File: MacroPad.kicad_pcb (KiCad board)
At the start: 2 copper layers, 3.6 x 3.3 mm, 42 parts, among them J1 Conn_01x04_Pin, SW1 SW_Push, SW10 SW_Push, SW11 SW_Push, SW12 SW_Push, SW13 RotaryEncoder_Switch, SW14 RotaryEncoder_Switch, SW2 SW_Push, SW3 SW_Push, SW4 SW_Push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

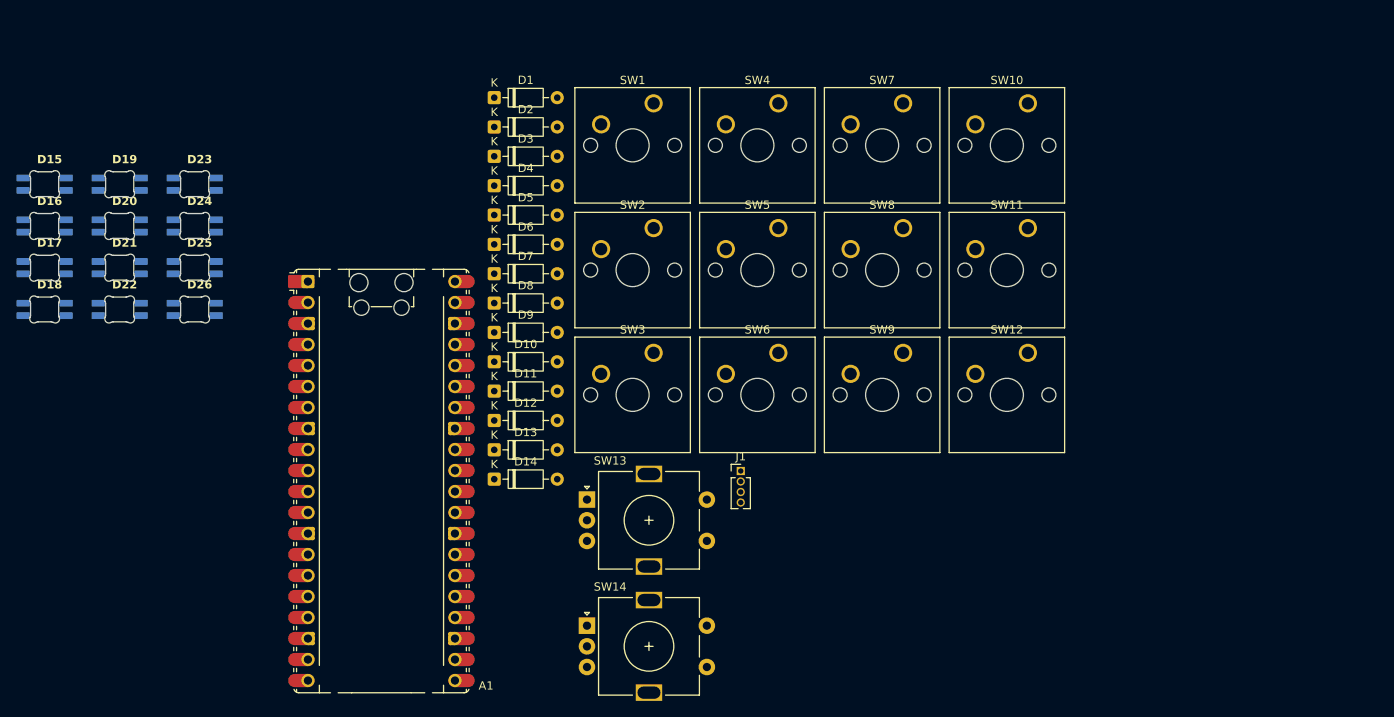
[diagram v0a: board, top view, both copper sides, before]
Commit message: Feat: Designed the PCB
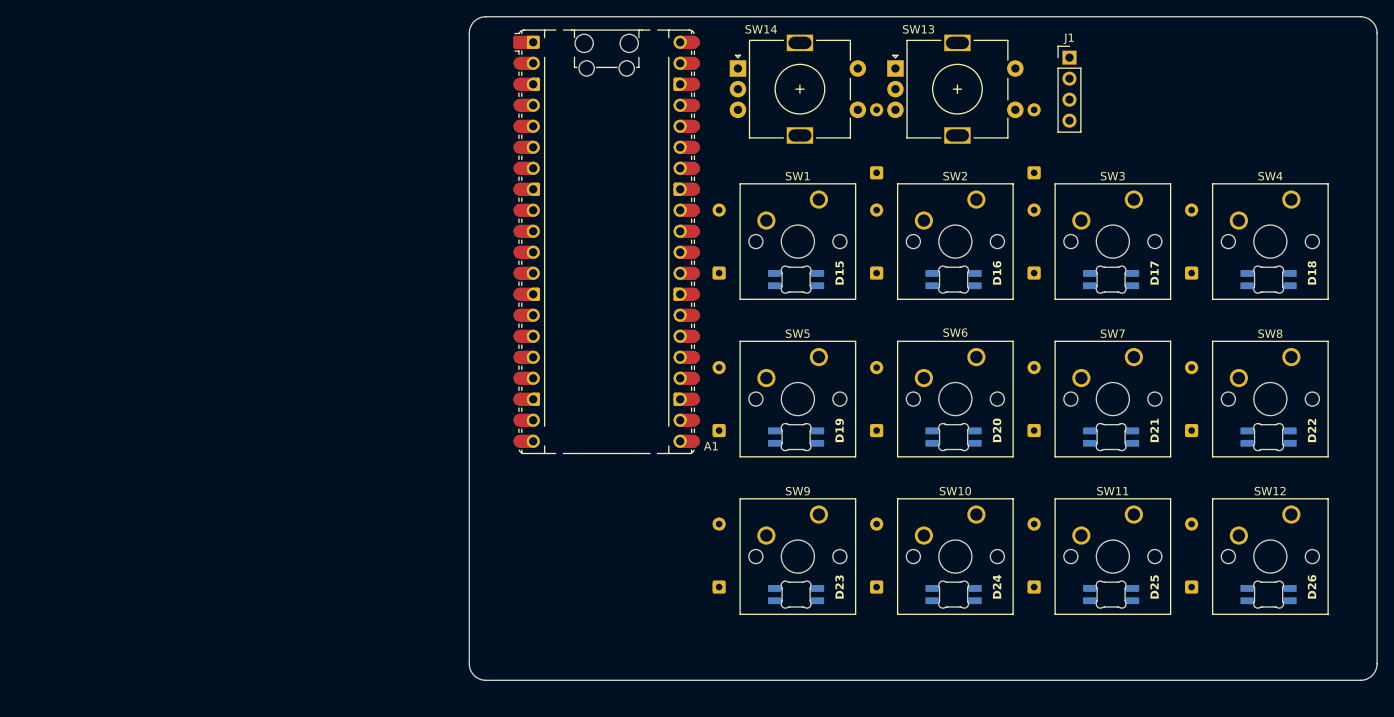
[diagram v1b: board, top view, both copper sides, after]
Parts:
- D1, D10, D11, D12, D13, D14, D2, D3, D4, D5, D6, D7, D8, D9: moved to B.Cu
- J1: footprint Connector_PinHeader_1.27mm:PinHeader_1x04_P1.27mm_Vertical -> Connector_PinHeader_2.54mm:PinHeader_1x04_P2.54mm_Vertical
- moved D18 148.1 mm to (193.4, 85.7)
- moved D22 139.8 mm to (193.4, 104.8)
- moved D26 134.4 mm to (193.4, 123.8)
- moved D17 129.0 mm to (174.4, 85.7)
- moved D21 121.7 mm to (174.4, 104.8)
- moved D25 117.7 mm to (174.4, 123.8)
- moved D16 110.1 mm to (155.3, 85.7)
- moved D20 104.1 mm to (155.3, 104.8)
- moved D24 102.1 mm to (155.3, 123.8)
- moved D15 91.6 mm to (136.3, 85.7)
- moved D23 88.1 mm to (136.3, 123.8)
- moved D19 87.4 mm to (136.3, 104.8)
- moved D12 86.7 mm to (184.1, 122.8), turned to 90 degrees
- moved D8 85.8 mm to (184.1, 103.9), turned to 90 degrees
- moved D4 85.0 mm to (184.1, 84.8), turned to 90 degrees
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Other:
- board size 3.6 x 3.3 mm -> 109.8 x 80.3 mm
